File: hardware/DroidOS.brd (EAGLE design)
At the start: 48.2 x 47.5 mm, 17 parts, among them J1 AUDIO_JACK_3.5MM_KIT, Q1 BC337

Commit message: Changed layout
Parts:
- J1: value AUDIO_JACK_3.5MM_KIT -> AUDIO_JACK_3.5MM
- U$1: value TEENSY_LC_DIL -> TEENSY_LC
- VREG: value (none) -> 5V
- moved SPK 17.5 mm to (62.3, 55.9), turned to 0 degrees
- moved R2 5.26 mm to (56.2, 64.3)
- moved VREG 4.98 mm to (90.2, 72.5), turned to 90 degrees
- moved SBUS/PPM 2.44 mm to (66.9, 60.6)
- moved SBUS_INV 2.44 mm to (66.9, 63.1)
- moved R1 1.79 mm to (61.0, 66.8)
- moved Q1 1.70 mm to (60.9, 62.2)
- moved J1 1.45 mm to (59.9, 76.0)
- moved PWM4 0.79 mm to (71.2, 69.3)
- moved PWM3 0.77 mm to (71.2, 71.9)
- moved PWM2 0.74 mm to (71.1, 74.4)
- moved PWM1 0.74 mm to (71.1, 77.0)
- moved SIG_SEL 0.59 mm to (76.7, 59.1)
- turned U$2 to 0 degrees
- renumbered + to VBAT+, - to VBAT-
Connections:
- net N$1 renamed DAC_R
- net N$10 renamed AUD_RX
- net N$11 renamed AUD_TX
- net N$12 renamed PWM2_SIG
- net N$13 renamed PWM4_SIG
- net N$14 renamed CTRL_SIG
- net N$15 renamed PWM3_SIG
- net N$16 renamed SBUS_INV_IN
- net N$18 renamed SBUS_INV_OUT
- net N$4 renamed SPK_R
- net N$5 renamed SBUS_OUT
- net N$6 renamed 3V+
- net N$7 renamed SPK_L
- net N$9 renamed PWM1_SIG
- removed net N$2: J1.TSH, U$2.DAC_L
- new net DAC_L: J1.TIP, U$2.DAC_L
- net GND: now also J1.SLEEVE, PWM4.3; no longer J1.RSH
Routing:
- net N$2: track 33.1 -> 0.00 mm
- net DAC_L: track 0.00 -> 29.7 mm
- net AUD_TX: track 30.2 -> 55.4 mm
- net SPK_R: track 4.39 -> 26.3 mm
- net 3V+: track 10.8 -> 31.7 mm
- net SPK_L: track 4.33 -> 19.1 mm
- net AUD_RX: track 35.9 -> 46.3 mm
- net PWM1_SIG: track 58.7 -> 53.2 mm
- net DAC_R: track 36.3 -> 31.8 mm
- net 5V: track 75.9 -> 79.8 mm
- net SBUS_INV_IN: track 4.31 -> 6.53 mm
- net VBAT: track 6.60 -> 8.43 mm
- net SBUS_OUT: track 11.9 -> 10.4 mm
- net PWM2_SIG: track 53.0 -> 51.7 mm
- net PWM3_SIG: track 23.5 -> 22.5 mm
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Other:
- outline, holes or cut-outs redrawn
- board text added: "1S-4S (MAX 16V)"
- board text added: "DroidOS v0.2 rev A J. Gennari 2017"
- board text added: "GND"
- board text added: "IN"
- board text added: "L"
- board text added: "OUT"
- board text added: "R"
- board text added: "SBUS/PPM"
- board text added: "SBUS_INV"

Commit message: v0.3
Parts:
- added PWR_SW: (no value), SparkFun-Connectors:1X02
- added R4: (no value), resistor:R0805
- added STATUS: (no value), led:SML0805
- moved SPK 1.91 mm to (60.4, 56.0)
- turned R2 to 90 degrees
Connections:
- new net N$1: PWR_SW.2, U$1.VIN
- new net N$2: R4.1, STATUS.A
- new net STATUS_LED: R4.2, U$1.21/A7
- net 5V: now also PWR_SW.1; no longer U$1.VIN
- net GND: now also STATUS.C
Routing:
- net STATUS_LED: track 0.00 -> 10.4 mm
- net PWM2_SIG: track 51.7 -> 61.5 mm
- net AUD_RX: track 46.3 -> 54.3 mm
- net N$1: track 0.00 -> 4.90 mm
- net N$2: track 0.00 -> 3.20 mm
- net AUD_TX: track 55.4 -> 52.6 mm
- net N$17: track 9.85 -> 11.3 mm
- net 5V: track 79.8 -> 81.1 mm
- net PWM1_SIG: track 53.2 -> 52.0 mm
- net SPK_R: track 26.3 -> 25.6 mm
- net SPK_L: track 19.1 -> 18.5 mm
- net DAC_L: track 29.7 -> 30.2 mm
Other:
- board text added: "DroidOS v0.3 rev D J. Gennari 2017"
- board text removed: "DroidOS v0.2 rev A J. Gennari 2017"

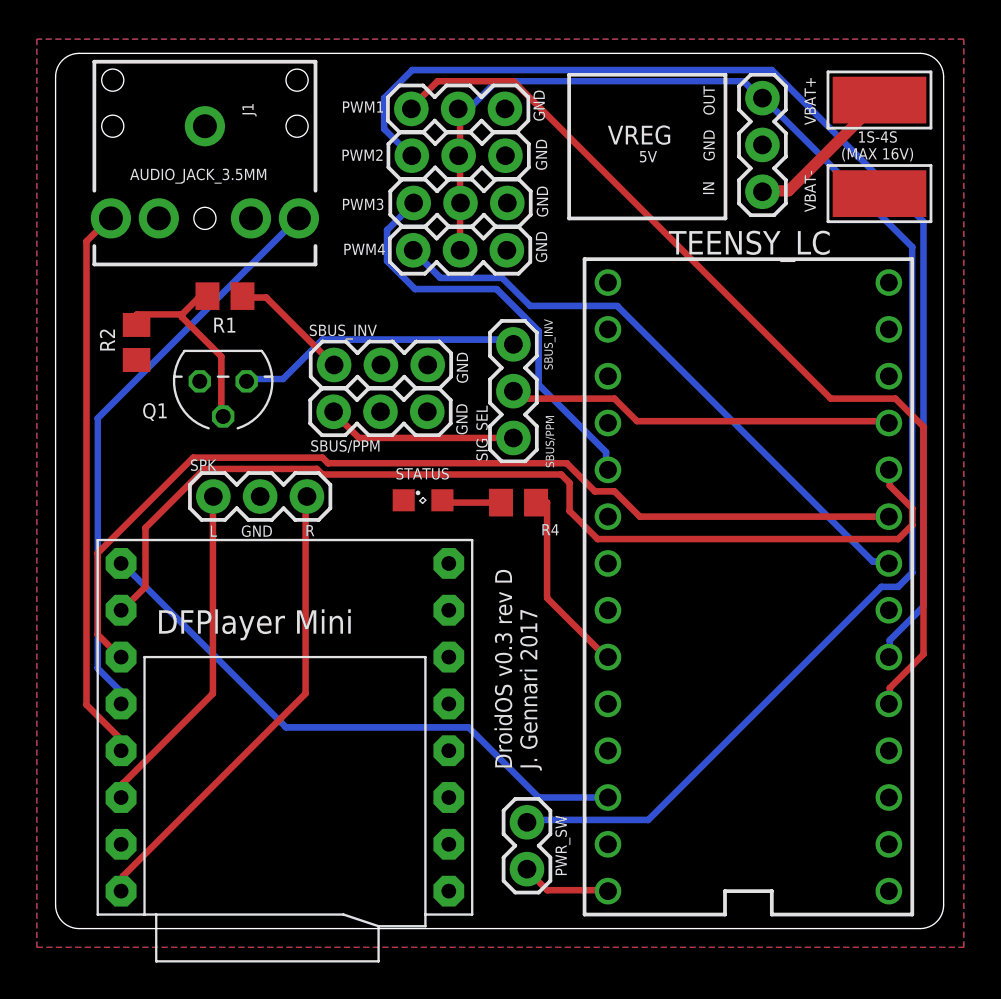
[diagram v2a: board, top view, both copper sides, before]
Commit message: Added SBUS power out
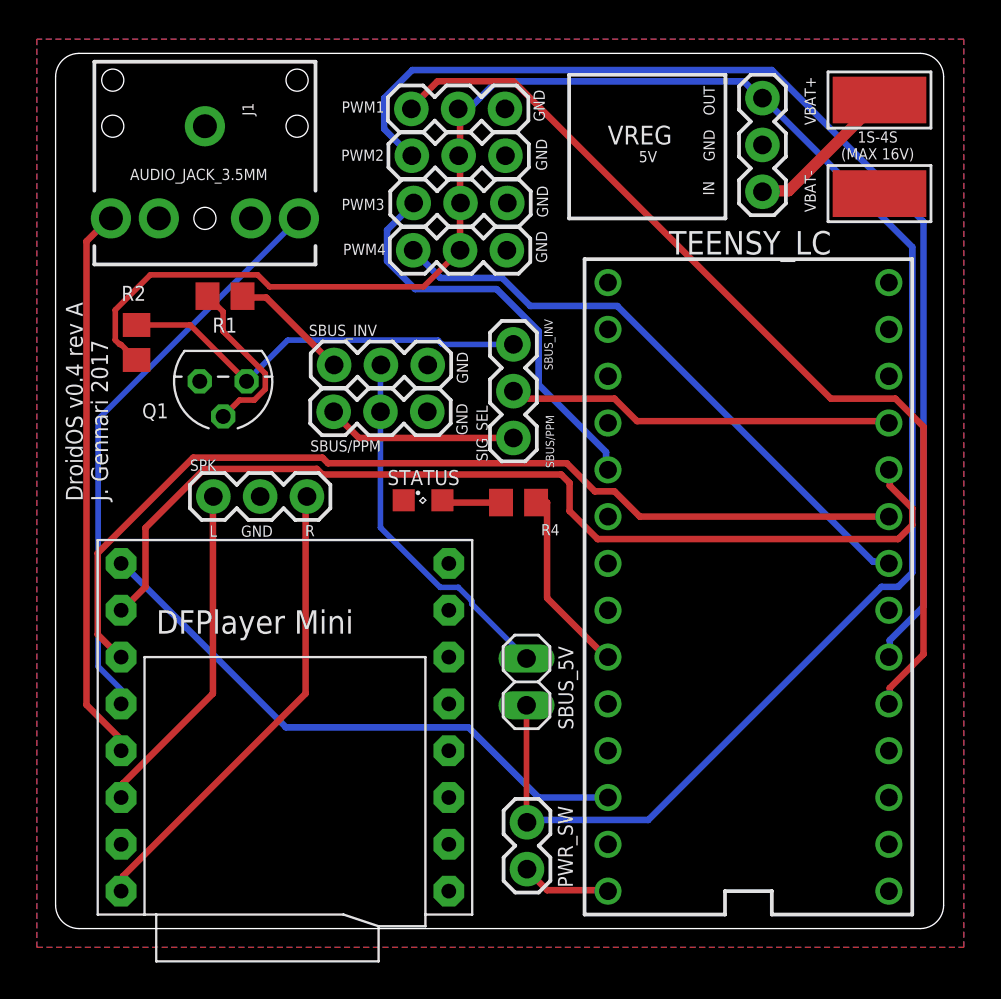
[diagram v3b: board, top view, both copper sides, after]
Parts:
- added SBUS_5V: (no value), pinhead:1X02
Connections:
- removed net N$17: Q1.2, R1.1, R2.2
- new net N$3: SBUS/PPM.2, SBUS_5V.2, SBUS_INV.2
- new net N$4: Q1.2, R1.1
- net 5V: now also R2.1, SBUS_5V.1
- net GND: no longer R2.1
- net SBUS_INV_OUT: now also R2.2
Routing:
- net 5V: track 81.1 -> 111.2 mm
- net N$3: track 0.00 -> 19.8 mm
- net N$17: track 11.3 -> 0.00 mm
- net N$4: track 0.00 -> 9.24 mm
- net SBUS_INV_OUT: track 15.7 -> 22.7 mm
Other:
- board text added: "DroidOS v0.4 rev A J. Gennari 2017"
- board text removed: "DroidOS v0.3 rev D J. Gennari 2017"
